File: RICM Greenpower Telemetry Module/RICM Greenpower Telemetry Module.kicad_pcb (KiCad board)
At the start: 2 copper layers, 80 x 95 mm, 57 parts, among them J0 Jack-DC, J1 Conn_01x04_Female, J10 Conn_01x05_Female, J2 Conn_01x02_Female, J3 Conn_01x02_Female, J4 Conn_01x02_Female, J5 Conn_01x02_Female, J6 Conn_01x02_Female, J7 Conn_01x03_Female, J8 Conn_01x03_Female, J9 Conn_01x04_Female, U1 XL2001E1, U2 MT92165, U3 Pico, U4 Adafruit_MicroSD_SPI_SDIO, U5 ADS7830, U6 MPU_6050_module

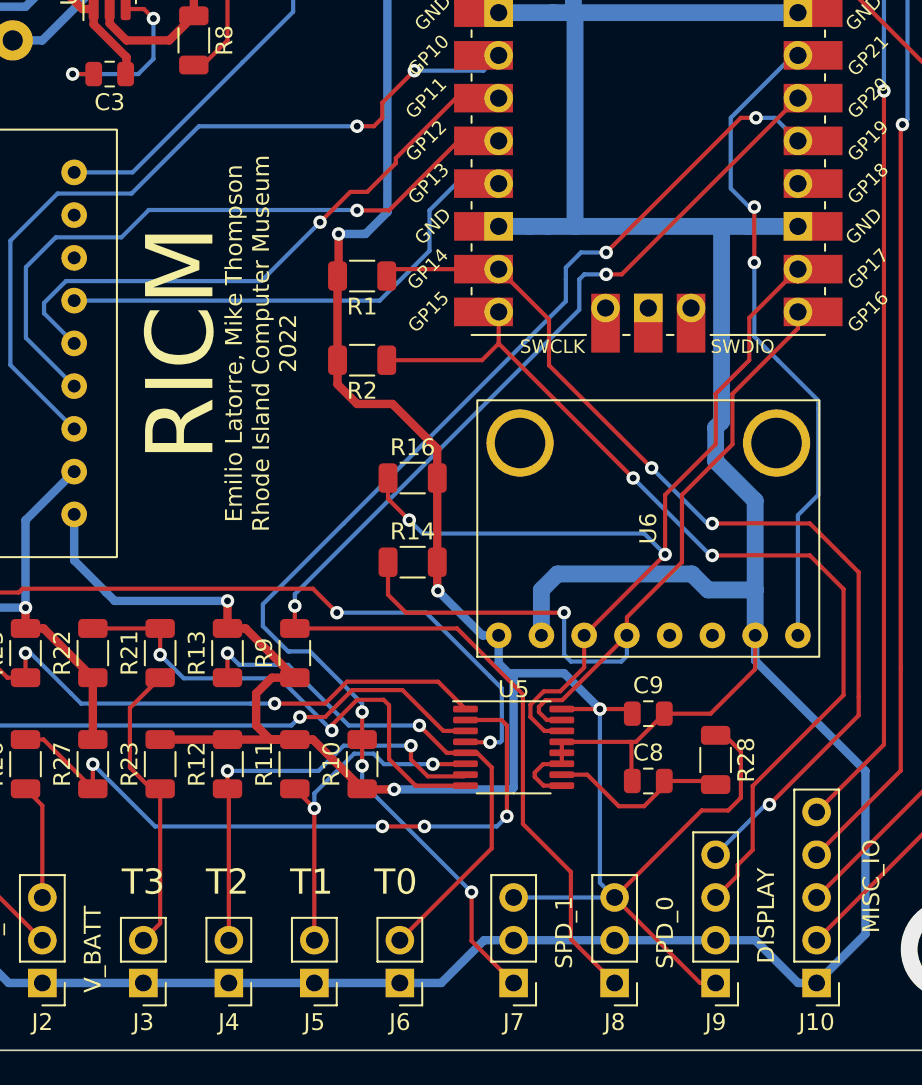
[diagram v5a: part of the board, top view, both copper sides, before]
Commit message: Schematic and layout corrections
Added revision silkscreen to schematic. Fixed pinout of display connector to match standard i2c pinout. Added schematic notes explaining resistor options for THERM_3.
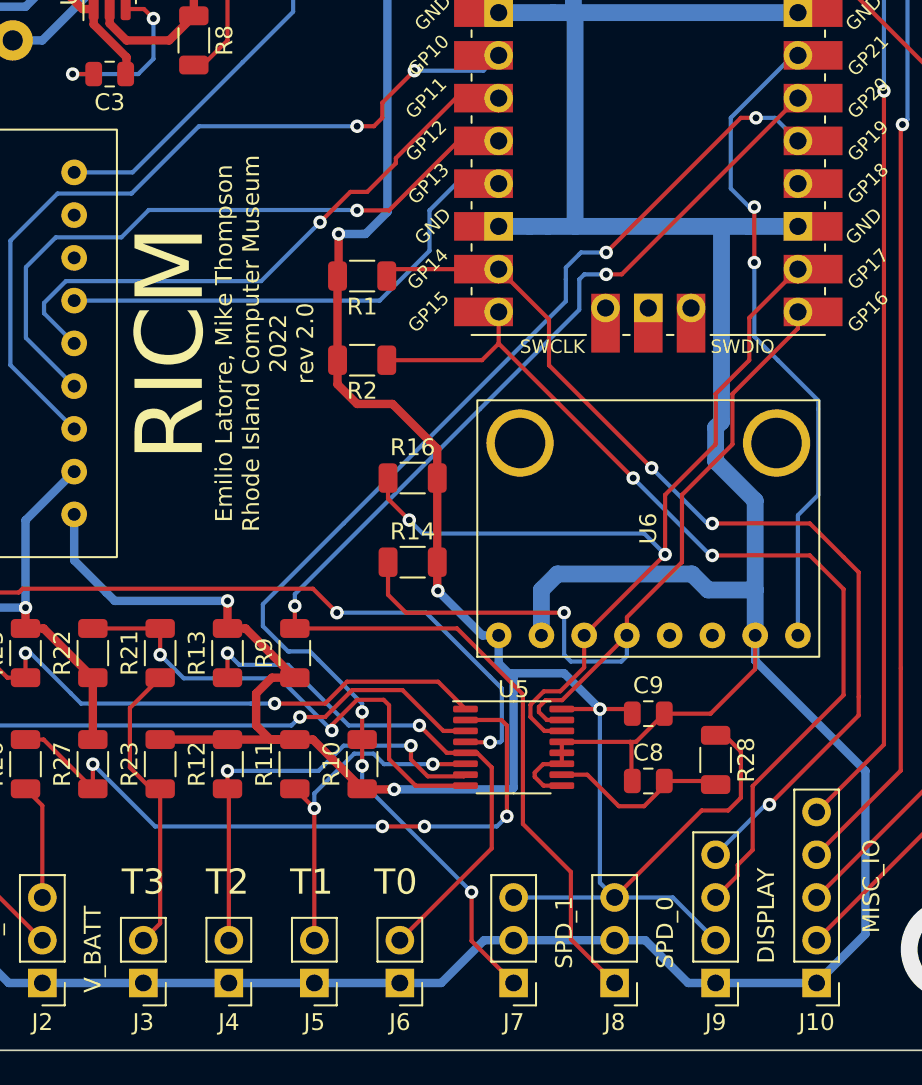
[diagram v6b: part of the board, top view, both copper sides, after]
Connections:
- J9 pad 1: +3V3 -> GND
- J9 pad 2: GND -> +3V3
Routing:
- net +3V3: track 188.8 -> 187.7 mm
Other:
- board text added: "Emilio Latorre, Mike Thompson Rhode Island Computer Museum 2022 rev 2.0"
- board text removed: "Emilio Latorre, Mike Thompson Rhode Island Computer Museum 2022"
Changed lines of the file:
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@@
     (pad_to_mask_clearance 0)
     (pcbplotparams
-      (layerselection 0x00010fc_ffffffff)
+      (layerselection 0x0000020_7fffffff)
       (disableapertmacros false)
       (usegerberextensions false)
@@
       (sketchpadsonfab false)
       (subtractmaskfromsilk false)
-      (outputformat 1)
+      (outputformat 4)
       (mirror false)
       (drillshape 0)
@@
     (fp_line (start -1.6 0.8) (end -1.6 -0.8) (layer "F.Fab") (width 0.1))
     (fp_line (start 1.6 0.8) (end -1.6 0.8) (layer "F.Fab") (width 0.1))
-    (pad "1" smd roundrect (at -1.4625 0 270) (size 1.125 1.75) (layers "F.Cu" "F.Paste" "F.Mask") (roundrect_rratio 0.222222)
+    (pad "1" smd roundrect (at -1.4625 0 270) (size 1.125 1.75) (layers "F.Cu" "F.Paste" "F.Mask") (roundrect_rratio 0.2222222222)
       (net 15 "+3V3") (pintype "passive"))
-    (pad "2" smd roundrect (at 1.4625 0 270) (size 1.125 1.75) (layers "F.Cu" "F.Paste" "F.Mask") (roundrect_rratio 0.222222)
+    (pad "2" smd roundrect (at 1.4625 0 270) (size 1.125 1.75) (layers "F.Cu" "F.Paste" "F.Mask") (roundrect_rratio 0.2222222222)
       (net 22 "Net-(C8-Pad2)") (pintype "passive"))
     (model "${KICAD6_3DMODEL_DIR}/Resistor_SMD.3dshapes/R_1206_3216Metric.wrl"
@@
     (fp_line (start 1.27 -1.27) (end 1.27 8.89) (layer "F.Fab") (width 0.1))
     (pad "1" thru_hole rect (at 0 0 180) (size 1.7 1.7) (drill 1) (layers *.Cu *.Mask)
-      (net 15 "+3V3") (pinfunction "Pin_1") (pintype "passive"))
+      (net 2 "GND") (pinfunction "Pin_1") (pintype "passive"))
     (pad "2" thru_hole oval (at 0 2.54 180) (size 1.7 1.7) (drill 1) (layers *.Cu *.Mask)
-      (net 2 "GND") (pinfunction "Pin_2") (pintype "passive"))
+      (net 15 "+3V3") (pinfunction "Pin_2") (pintype "passive"))
     (pad "3" thru_hole oval (at 0 5.08 180) (size 1.7 1.7) (drill 1) (layers *.Cu *.Mask)
       (net 23 "I2C1_SCL") (pinfunction "Pin_3") (pintype "passive"))
@@
     (effects (font (size 1 1) (thickness 0.15)))
   )
-  (gr_text "Emilio Latorre, Mike Thompson\nRhode Island Computer Museum\n2022" (at 45 65 90) (layer "F.SilkS")
+  (gr_text "Emilio Latorre, Mike Thompson\nRhode Island Computer Museum\n2022\nrev 2.0" (at 45.212 65 90) (layer "F.SilkS")
     (effects (font (size 1 1) (thickness 0.15)))
   )
@@
     (effects (font (size 1.5 1.5) (thickness 0.3)))
   )
-  (gr_text "RICM" (at 40.25 65 90) (layer "F.SilkS")
+  (gr_text "RICM" (at 39.624 65 90) (layer "F.SilkS")
     (effects (font (size 4 4) (thickness 0.5)))
   )
@@
   (segment (start 60 100.46) (end 58.24 100.46) (width 0.5) (layer "B.Cu") (net 2))
   (segment (start 63.55 32.75) (end 63.55 45.25) (width 1) (layer "B.Cu") (net 2))
-  (segment (start 74.36 100.46) (end 72 100.46) (width 0.5) (layer "B.Cu") (net 2))
+  (segment (start 72 103) (end 78 103) (width 0.5) (layer "B.Cu") (net 2))
   (segment (start 16.9 94.7) (end 15.9 94.7) (width 0.5) (layer "B.Cu") (net 2))
   (segment (start 26.847349 15.152651) (end 28 15.152651) (width 1.5) (layer "B.Cu") (net 2))
@@
   (segment (start 59.11 58.05) (end 60.95 58.05) (width 1) (layer "B.Cu") (net 2))
   (segment (start 28 15.152651) (end 37.752651 15.152651) (width 1.5) (layer "B.Cu") (net 2))
+  (segment (start 66 100.46) (end 67.821 100.46) (width 0.5) (layer "B.Cu") (net 2))
   (segment (start 62 20) (end 61.95 19.95) (width 1) (layer "B.Cu") (net 2))
   (segment (start 19 80.7) (end 31 80.7) (width 0.5) (layer "B.Cu") (net 2))
@@
   (segment (start 48.4 37.7) (end 48.4 34) (width 0.5) (layer "B.Cu") (net 2))
   (segment (start 18 26.152651) (end 18 24) (width 1.5) (layer "B.Cu") (net 2))
+  (segment (start 67.821 100.46) (end 70.361 103) (width 0.5) (layer "B.Cu") (net 2))
   (segment (start 61.65 79.65) (end 62.600489 78.699511) (width 1) (layer "B.Cu") (net 2))
   (segment (start 43.65 21.05) (end 49.95 21.05) (width 1.5) (layer "B.Cu") (net 2))
@@
   (segment (start 63.55 45.25) (end 63.65 45.35) (width 1) (layer "B.Cu") (net 2))
   (segment (start 62.05 19.95) (end 63.55 19.95) (width 1) (layer "B.Cu") (net 2))
+  (segment (start 70.361 103) (end 72 103) (width 0.5) (layer "B.Cu") (net 2))
   (segment (start 72.35 69.65) (end 72 70) (width 1) (layer "B.Cu") (net 2))
   (segment (start 72 70) (end 72 72) (width 1) (layer "B.Cu") (net 2))
   (segment (start 70.599511 78.699511) (end 71.55 79.65) (width 1) (layer "B.Cu") (net 2))
-  (segment (start 66 100.46) (end 72 100.46) (width 0.5) (layer "B.Cu") (net 2))
-  (segment (start 76.9 103) (end 74.36 100.46) (width 0.5) (layer "B.Cu") (net 2))
   (segment (start 32 103) (end 38 103) (width 0.5) (layer "B.Cu") (net 2))
   (segment (start 31 75.51) (end 33.89 72.62) (width 0.5) (layer "B.Cu") (net 2))
@@
   (segment (start 26 100.46) (end 24.16 100.46) (width 0.5) (layer "B.Cu") (net 2))
   (segment (start 59.11 32.65) (end 63.45 32.65) (width 1) (layer "B.Cu") (net 2))
-  (segment (start 78 103) (end 76.9 103) (width 0.5) (layer "B.Cu") (net 2))
   (segment (start 61.95 19.95) (end 59.11 19.95) (width 1) (layer "B.Cu") (net 2))
   (segment (start 31 80.7) (end 31 75.51) (width 0.5) (layer "B.Cu") (net 2))
@@
   (segment (start 50.7 68.6) (end 49.5375 67.4375) (width 0.5) (layer "F.Cu") (net 15))
   (segment (start 62.8625 86.725) (end 66.775 86.725) (width 0.25) (layer "F.Cu") (net 15))
-  (segment (start 66 97.92) (end 71.08 103) (width 0.25) (layer "F.Cu") (net 15))
   (segment (start 51.0375 91.5) (end 51 91.4625) (width 0.5) (layer "F.Cu") (net 15))
   (segment (start 49.5375 66) (end 49.5375 61) (width 0.5) (layer "F.Cu") (net 15))
@@
   (segment (start 38 40.05) (end 36.95 39) (width 0.5) (layer "F.Cu") (net 15))
   (segment (start 55.4625 78) (end 55.4625 79.6625) (width 0.5) (layer "F.Cu") (net 15))
-  (segment (start 71.08 103) (end 72 103) (width 0.25) (layer "F.Cu") (net 15))
   (segment (start 49.6 58.5) (end 49.6 60.9375) (width 0.5) (layer "F.Cu") (net 15))
   (segment (start 39 88.5375) (end 43 88.5375) (width 0.5) (layer "F.Cu") (net 15))
@@
   (segment (start 33.89 75.16) (end 33.89 77.89) (width 0.5) (layer "B.Cu") (net 15))
   (segment (start 51.4 38.5) (end 52.5 39.6) (width 0.5) (layer "B.Cu") (net 15))
+  (segment (start 66 97.92) (end 69.46 97.92) (width 0.25) (layer "B.Cu") (net 15))
   (segment (start 52.5 57.2) (end 51.2 58.5) (width 0.5) (layer "B.Cu") (net 15))
   (segment (start 35.8 79.8) (end 36.3 80.3) (width 0.5) (layer "B.Cu") (net 15))
@@
   (segment (start 52.9 91.5) (end 59.9 91.5) (width 0.5) (layer "B.Cu") (net 15))
   (segment (start 59.11 84.01) (end 59.7 84.6) (width 0.5) (layer "B.Cu") (net 15))
+  (segment (start 69.46 97.92) (end 72 100.46) (width 0.25) (layer "B.Cu") (net 15))
   (segment (start 59.9 91.5) (end 60 91.4) (width 0.5) (layer "B.Cu") (net 15))
   (segment (start 60 84.8) (end 59.8 84.6) (width 0.5) (layer "B.Cu") (net 15))
